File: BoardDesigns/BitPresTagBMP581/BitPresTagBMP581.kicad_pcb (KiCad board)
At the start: 4 copper layers, 18 x 10 mm, 26 parts, among them J201 CONN_02X04, J301 Conn_01x01, J302 Conn_01x01, J303 Conn_01x01, J304 Conn_01x01, J401 CONN_01X02, Q501 Q_NPN_BEC, U1 at25ex321D-UUN, U2 ADXL367BCCZ-RL7, U3 BMP585, U302 stm32l431kc, U501 RV-3028-C8

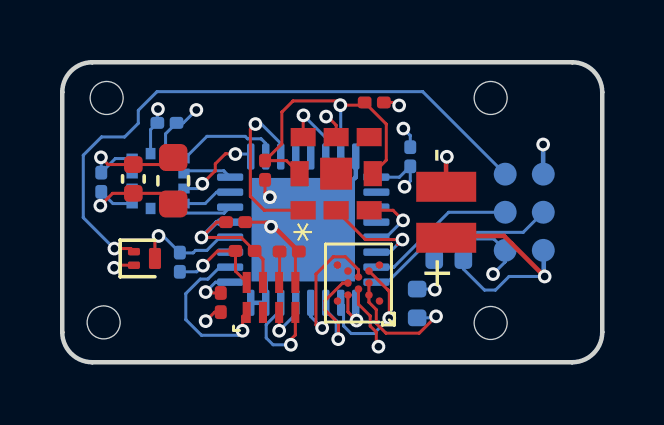
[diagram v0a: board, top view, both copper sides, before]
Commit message: added smps breakout board
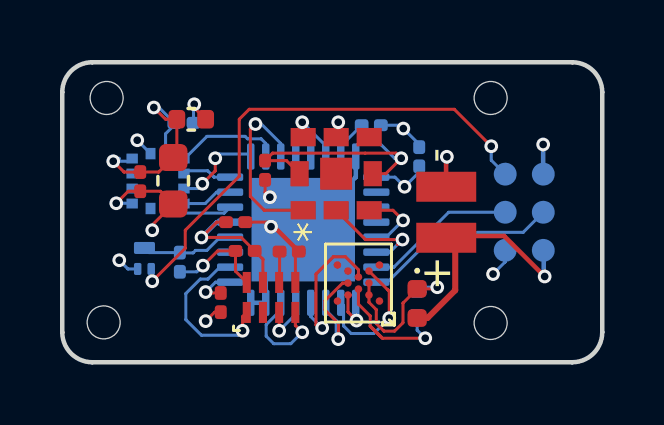
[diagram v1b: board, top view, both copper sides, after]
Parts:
- C3: moved to B.Cu
- C7, D401: moved to F.Cu
- Q501: value Q_NPN_BEC -> PMBT2222AMBYL; moved to B.Cu
- U501: value RV-3028-C8 -> RV-3028-C8-32.768kHz-1PPM-TA-QC
- moved C404 2.77 mm to (144.3, 104.9), turned to 0 degrees
- moved D401 1.81 mm to (151.8, 111.0), turned to -90 degrees
- moved C7 1.30 mm to (142.6, 107.0)
- moved C3 0.77 mm to (150.3, 105.1)
- moved C1 0.56 mm to (144.1, 105.0), turned to 0 degrees
- moved C2 0.30 mm to (151.9, 106.2)
- turned C4 to -90 degrees
- turned Q501 to 90 degrees
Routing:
- net RST: track 20.6 -> 17.2 mm, vias 1 -> 2
- net GND: track 33.1 -> 34.9 mm
- net VIN: track 23.7 -> 22.6 mm
- net Net-(Q501-C): track 3.98 -> 3.49 mm, vias 1 -> 0

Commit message: checkpoint
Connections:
- U3 pad 5: unconnected-(U3-INT-Pad5) -> /lps_rdy
- U302 pad 12: unconnected-(U302-PA6-Pad12) -> /lps_rdy
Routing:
- net /lps_rdy: track 0.00 -> 5.05 mm, vias 0 -> 1
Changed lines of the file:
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@@
 			(size 0.8382 0.6096)
 			(layers "F.Cu" "F.Mask" "F.Paste")
-			(net "unconnected-(U3-INT-Pad5)")
+			(net "/lps_rdy")
 			(pinfunction "INT_5")
 			(pintype "output")
@@
 			(layers "B.Cu" "B.Mask" "B.Paste")
 			(roundrect_rratio 0.25)
-			(net "unconnected-(U302-PA6-Pad12)")
+			(net "/lps_rdy")
 			(pinfunction "PA6_12")
 			(pintype "bidirectional")
@@
 			(net "unconnected-(U302-PA7-Pad13)")
 			(pinfunction "PA7_13")
-			(pintype "bidirectional")
+			(pintype "bidirectional+no_connect")
 		)
 		(pad "14" smd roundrect
@@
 			(net "unconnected-(U302-PA8-Pad18)")
 			(pinfunction "PA8_18")
-			(pintype "bidirectional")
+			(pintype "bidirectional+no_connect")
 		)
 		(pad "19" smd roundrect
@@
 			(net "unconnected-(U302-PA9-Pad19)")
 			(pinfunction "PA9_19")
-			(pintype "bidirectional")
+			(pintype "bidirectional+no_connect")
 		)
 		(pad "20" smd roundrect
@@
 			(net "unconnected-(U302-PA10-Pad20)")
 			(pinfunction "PA10_20")
-			(pintype "bidirectional")
+			(pintype "bidirectional+no_connect")
 		)
 		(pad "21" smd roundrect
@@
 	)
 	(segment
-		(start 143 110.3)
-		(end 144.1 109.2)
-		(width 0.1016)
-		(layer "F.Cu")
-		(net "RST")
-	)
-	(segment
-		(start 144.1 109.2)
-		(end 144.1 108.6)
-		(width 0.1016)
-		(layer "F.Cu")
-		(net "RST")
-	)
-	(segment
-		(start 153.0682 104.5682)
-		(end 154.3 105.8)
-		(width 0.1016)
-		(layer "F.Cu")
-		(net "RST")
-	)
-	(segment
-		(start 144.1 108.6)
-		(end 145.9 106.8)
-		(width 0.1016)
-		(layer "F.Cu")
-		(net "RST")
-	)
-	(segment
-		(start 145.9 104.9)
-		(end 146.2318 104.5682)
-		(width 0.1016)
-		(layer "F.Cu")
-		(net "RST")
-	)
-	(segment
-		(start 146.2318 104.5682)
-		(end 153.0682 104.5682)
-		(width 0.1016)
-		(layer "F.Cu")
-		(net "RST")
-	)
-	(segment
-		(start 145.9 106.8)
-		(end 145.9 104.9)
-		(width 0.1016)
-		(layer "F.Cu")
-		(net "RST")
-	)
-	(via
-		(at 143 110.3)
-		(size 0.4572)
-		(drill 0.254)
-		(layers "F.Cu" "B.Cu")
-		(net "RST")
-	)
-	(via
-		(at 154.3 105.8)
-		(size 0.4572)
-		(drill 0.254)
-		(layers "F.Cu" "B.Cu")
-		(net "RST")
-	)
-	(segment
-		(start 142.965 109.89)
-		(end 142.965 110.265)
-		(width 0.1016)
-		(layer "B.Cu")
-		(net "RST")
-	)
-	(segment
-		(start 142.965 110.265)
-		(end 143 110.3)
-		(width 0.1016)
-		(layer "B.Cu")
-		(net "RST")
-	)
-	(segment
-		(start 154.765 106.73)
-		(end 154.3 106.265)
-		(width 0.1016)
-		(layer "B.Cu")
-		(net "RST")
-	)
-	(segment
-		(start 154.3 106.265)
-		(end 154.3 105.8)
-		(width 0.1016)
-		(layer "B.Cu")
-		(net "RST")
-	)
-	(segment
-		(start 144.360658 109.355)
-		(end 143.95 109.355)
-		(width 0.1016)
-		(layer "B.Cu")
-		(net "Net-(Q501-C)")
-	)
-	(segment
-		(start 144.443846 109.271812)
-		(end 144.360658 109.355)
-		(width 0.1016)
-		(layer "B.Cu")
-		(net "Net-(Q501-C)")
-	)
-	(segment
-		(start 144.81999 109.271812)
-		(end 144.443846 109.271812)
-		(width 0.1016)
-		(layer "B.Cu")
-		(net "Net-(Q501-C)")
-	)
-	(segment
-		(start 145.2177 108.83)
-		(end 145.596042 108.83)
-		(width 0.1016)
-		(layer "B.Cu")
-		(net "Net-(Q501-C)")
-	)
-	(segment
-		(start 142.895 109.345)
-		(end 142.74 109.19)
-		(width 0.1016)
-		(layer "B.Cu")
-		(net "Net-(Q501-C)")
-	)
-	(segment
-		(start 143.92 109.345)
-		(end 142.895 109.345)
-		(width 0.1016)
-		(layer "B.Cu")
-		(net "Net-(Q501-C)")
-	)
-	(segment
-		(start 145.261802 108.83)
-		(end 144.81999 109.271812)
-		(width 0.1016)
-		(layer "B.Cu")
-		(net "Net-(Q501-C)")
-	)
-	(segment
-		(start 145.596042 108.83)
-		(end 145.261802 108.83)
-		(width 0.1016)
-		(layer "B.Cu")
-		(net "Net-(Q501-C)")
-	)
-	(segment
 		(start 150.3492 106.715)
 		(end 150.785 106.715)
@@
 	)
 	(segment
+		(start 147.736974 104.365)
+		(end 149.463026 104.365)
+		(width 0.1016)
+		(layer "F.Cu")
+		(net "RST")
+	)
+	(segment
+		(start 146.827458 104.5682)
+		(end 146.979058 104.4166)
+		(width 0.1016)
+		(layer "F.Cu")
+		(net "RST")
+	)
+	(segment
+		(start 153.0682 104.5682)
+		(end 154.3 105.8)
+		(width 0.1016)
+		(layer "F.Cu")
+		(net "RST")
+	)
+	(segment
+		(start 146.2318 104.5682)
+		(end 146.827458 104.5682)
+		(width 0.1016)
+		(layer "F.Cu")
+		(net "RST")
+	)
+	(segment
+		(start 149.463026 104.365)
+		(end 149.666226 104.5682)
+		(width 0.1016)
+		(layer "F.Cu")
+		(net "RST")
+	)
+	(segment
+		(start 145.9 104.9)
+		(end 146.2318 104.5682)
+		(width 0.1016)
+		(layer "F.Cu")
+		(net "RST")
+	)
+	(segment
+		(start 145.9 106.8)
+		(end 145.9 104.9)
+		(width 0.1016)
+		(layer "F.Cu")
+		(net "RST")
+	)
+	(segment
+		(start 144.1 108.6)
+		(end 145.9 106.8)
+		(width 0.1016)
+		(layer "F.Cu")
+		(net "RST")
+	)
+	(segment
+		(start 143 110.3)
+		(end 144.1 109.2)
+		(width 0.1016)
+		(layer "F.Cu")
+		(net "RST")
+	)
+	(segment
+		(start 149.666226 104.5682)
+		(end 153.0682 104.5682)
+		(width 0.1016)
+		(layer "F.Cu")
+		(net "RST")
+	)
+	(segment
+		(start 146.979058 104.4166)
+		(end 147.685374 104.4166)
+		(width 0.1016)
+		(layer "F.Cu")
+		(net "RST")
+	)
+	(segment
+		(start 144.1 109.2)
+		(end 144.1 108.6)
+		(width 0.1016)
+		(layer "F.Cu")
+		(net "RST")
+	)
+	(segment
+		(start 147.685374 104.4166)
+		(end 147.736974 104.365)
+		(width 0.1016)
+		(layer "F.Cu")
+		(net "RST")
+	)
+	(via
+		(at 143 110.3)
+		(size 0.4572)
+		(drill 0.254)
+		(layers "F.Cu" "B.Cu")
+		(net "RST")
+	)
+	(via
+		(at 154.3 105.8)
+		(size 0.4572)
+		(drill 0.254)
+		(layers "F.Cu" "B.Cu")
+		(net "RST")
+	)
+	(segment
+		(start 142.965 109.89)
+		(end 142.965 110.265)
+		(width 0.1016)
+		(layer "B.Cu")
+		(net "RST")
+	)
+	(segment
+		(start 142.965 110.265)
+		(end 143 110.3)
+		(width 0.1016)
+		(layer "B.Cu")
+		(net "RST")
+	)
+	(segment
+		(start 154.765 106.73)
+		(end 154.3 106.265)
+		(width 0.1016)
+		(layer "B.Cu")
+		(net "RST")
+	)
+	(segment
+		(start 154.3 106.265)
+		(end 154.3 105.8)
+		(width 0.1016)
+		(layer "B.Cu")
+		(net "RST")
+	)
+	(segment
+		(start 144.360658 109.355)
+		(end 143.95 109.355)
+		(width 0.1016)
+		(layer "B.Cu")
+		(net "Net-(Q501-C)")
+	)
+	(segment
+		(start 144.443846 109.271812)
+		(end 144.360658 109.355)
+		(width 0.1016)
+		(layer "B.Cu")
+		(net "Net-(Q501-C)")
+	)
+	(segment
+		(start 144.81999 109.271812)
+		(end 144.443846 109.271812)
+		(width 0.1016)
+		(layer "B.Cu")
+		(net "Net-(Q501-C)")
+	)
+	(segment
+		(start 145.2177 108.83)
+		(end 145.596042 108.83)
+		(width 0.1016)
+		(layer "B.Cu")
+		(net "Net-(Q501-C)")
+	)
+	(segment
+		(start 142.895 109.345)
+		(end 142.74 109.19)
+		(width 0.1016)
+		(layer "B.Cu")
+		(net "Net-(Q501-C)")
+	)
+	(segment
+		(start 143.92 109.345)
+		(end 142.895 109.345)
+		(width 0.1016)
+		(layer "B.Cu")
+		(net "Net-(Q501-C)")
+	)
+	(segment
+		(start 145.261802 108.83)
+		(end 144.81999 109.271812)
+		(width 0.1016)
+		(layer "B.Cu")
+		(net "Net-(Q501-C)")
+	)
+	(segment
+		(start 145.596042 108.83)
+		(end 145.261802 108.83)
+		(width 0.1016)
+		(layer "B.Cu")
+		(net "Net-(Q501-C)")
+	)
+	(segment
 		(start 145.596042 107.83)
 		(end 145.398541 108.027501)
@@
 		(net "/ACCEL_SCK")
 	)
+	(segment
+		(start 149.378858 104.5682)
+		(end 150.23 105.419342)
+		(width 0.1016)
+		(layer "F.Cu")
+		(net "/lps_rdy")
+	)
+	(segment
+		(start 147.821142 104.5682)
+		(end 149.378858 104.5682)
+		(width 0.1016)
+		(layer "F.Cu")
+		(net "/lps_rdy")
+	)
+	(segment
+		(start 147.439342 104.95)
+		(end 147.821142 104.5682)
+		(width 0.1016)
+		(layer "F.Cu")
+		(net "/lps_rdy")
+	)
+	(segment
+		(start 150.23 105.419342)
+		(end 150.23 105.4958)
+		(width 0.1016)
+		(layer "F.Cu")
+		(net "/lps_rdy")
+	)
+	(segment
+		(start 147.2 104.95)
+		(end 147.439342 104.95)
+		(width 0.1016)
+		(layer "F.Cu")
+		(net "/lps_rdy")
+	)
+	(via
+		(at 147.2 104.95)
+		(size 0.4572)
+		(drill 0.254)
+		(layers "F.Cu" "B.Cu")
+		(net "/lps_rdy")
+	)
+	(segment
+		(start 147.783542 105.533542)
+		(end 147.2 104.95)
+		(width 0.1016)
+		(layer "B.Cu")
+		(net "/lps_rdy")
+	)
+	(segment
+		(start 147.783542 106.1425)
+		(end 147.783542 105.533542)
+		(width 0.1016)
+		(layer "B.Cu")
+		(net "/lps_rdy")
+	)
 	(zone
